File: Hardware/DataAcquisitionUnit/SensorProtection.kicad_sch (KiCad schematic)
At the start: 0 parts

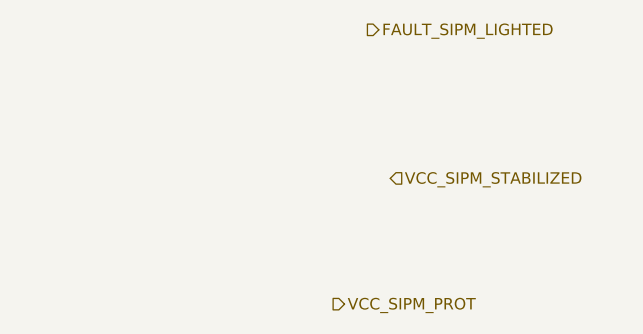
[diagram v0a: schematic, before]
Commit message: fix: #129, fix: #127
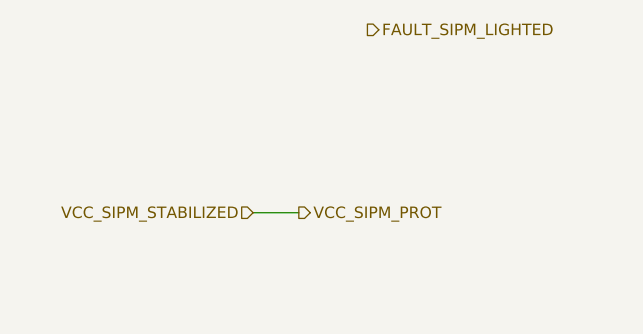
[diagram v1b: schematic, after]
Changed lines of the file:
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@@
 	(generator_version "10.0")
 	(paper "A4")
+	(wire
+		(pts
+			(xy 110.49 113.03) (xy 115.57 113.03)
+		)
+		(stroke
+			(width 0)
+			(type default)
+		)
+	)
 	(hierarchical_label "VCC_SIPM_STABILIZED"
 		(shape input)
-		(at 125.73 109.22 0)
+		(at 110.49 113.03 180)
 		(effects
 			(font
 				(size 1.27 1.27)
 			)
-			(justify left)
+			(justify right)
 		)
 	)
 	(hierarchical_label "VCC_SIPM_PROT"
 		(shape output)
-		(at 119.38 123.19 0)
+		(at 115.57 113.03 0)
 		(effects
 			(font
